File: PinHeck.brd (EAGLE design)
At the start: 359.2 x 152.3 mm, 338 parts, among them IC1 FT232RQ, IC2 PIC32MX7X5FL-PT, IC3 CD74HCT244E, IC4 CD74HCT244E, IC5 ULN2803A, J1 500075-1517, J11 No Load, J2 500075-1517, J6 161-3507-E, P1 TC33X-2-103E, SW1 101-0134-EV, SW2 101-0134-EV, U1 P8X32A-Q44, U10 74HCT2G04GV,125, U11 74HC165D,652, U12 74HC165D,652, U14 MC74HC08ADG, U15 MC74HC08ADG, U16 MC74HC08ADG, U17 MC74HC08ADG, U18 MC74HC08ADG, U19 MC74HC08ADG, U2 FT230X, U20 TIP107, U21 TIP107, U22 TIP107, U23 TIP107, U24 TIP107, U25 TIP107, U26 TIP107, U27 TIP107, U28 TIP102, U29 TIP102, U3 74HC595D-Q100, U30 TIP102, U31 TIP102, U32 TIP102, U33 TIP102, U34 TIP102, U35 TIP102, U36 WS2801, U37 TIP102, U38 WS2801, U4 CAT24M01XI-T2, U40 TIP102, U41 TIP102, U42 TIP102, U43 TIP102, U44 TIP102, U45 TIP102, U46 TIP102, U47 TIP102, U48 TIP102, U49 TIP102, U5 74HC595D-Q100, U50 TIP102, U51 TIP102, U52 CD74HC123M96, U6 TIP102, U7 TIP102, U8 TIP102, U9 TIP102, X1 FQ7050B-8.000, X2 ECS-65-20-4X

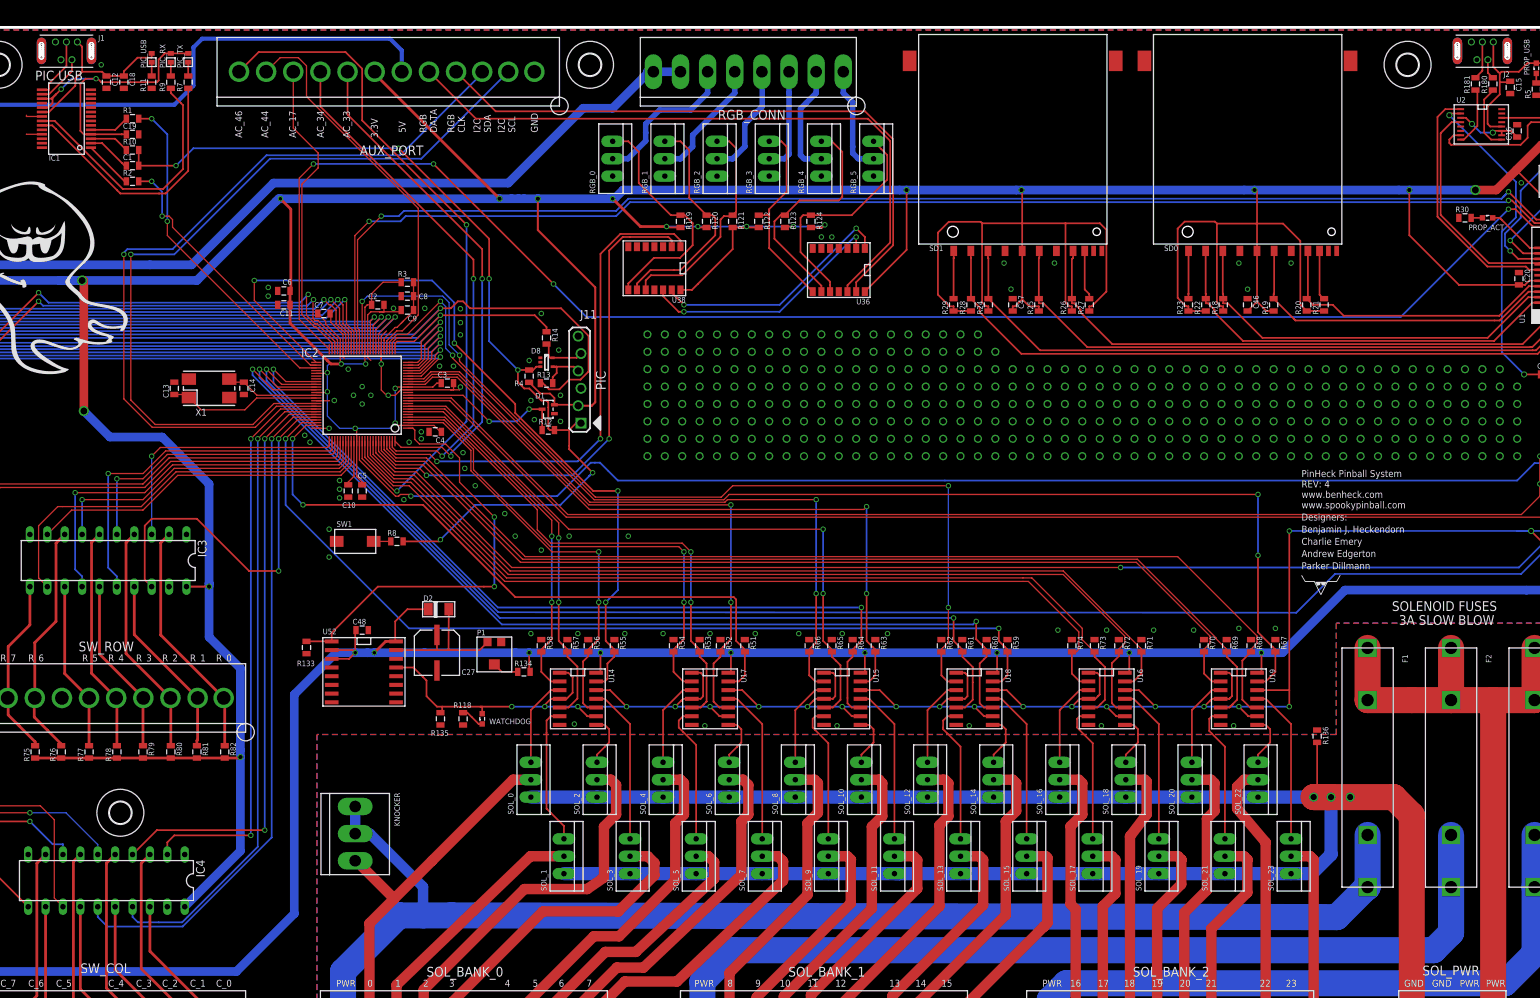
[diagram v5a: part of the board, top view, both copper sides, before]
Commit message: Fixed spacing errors.
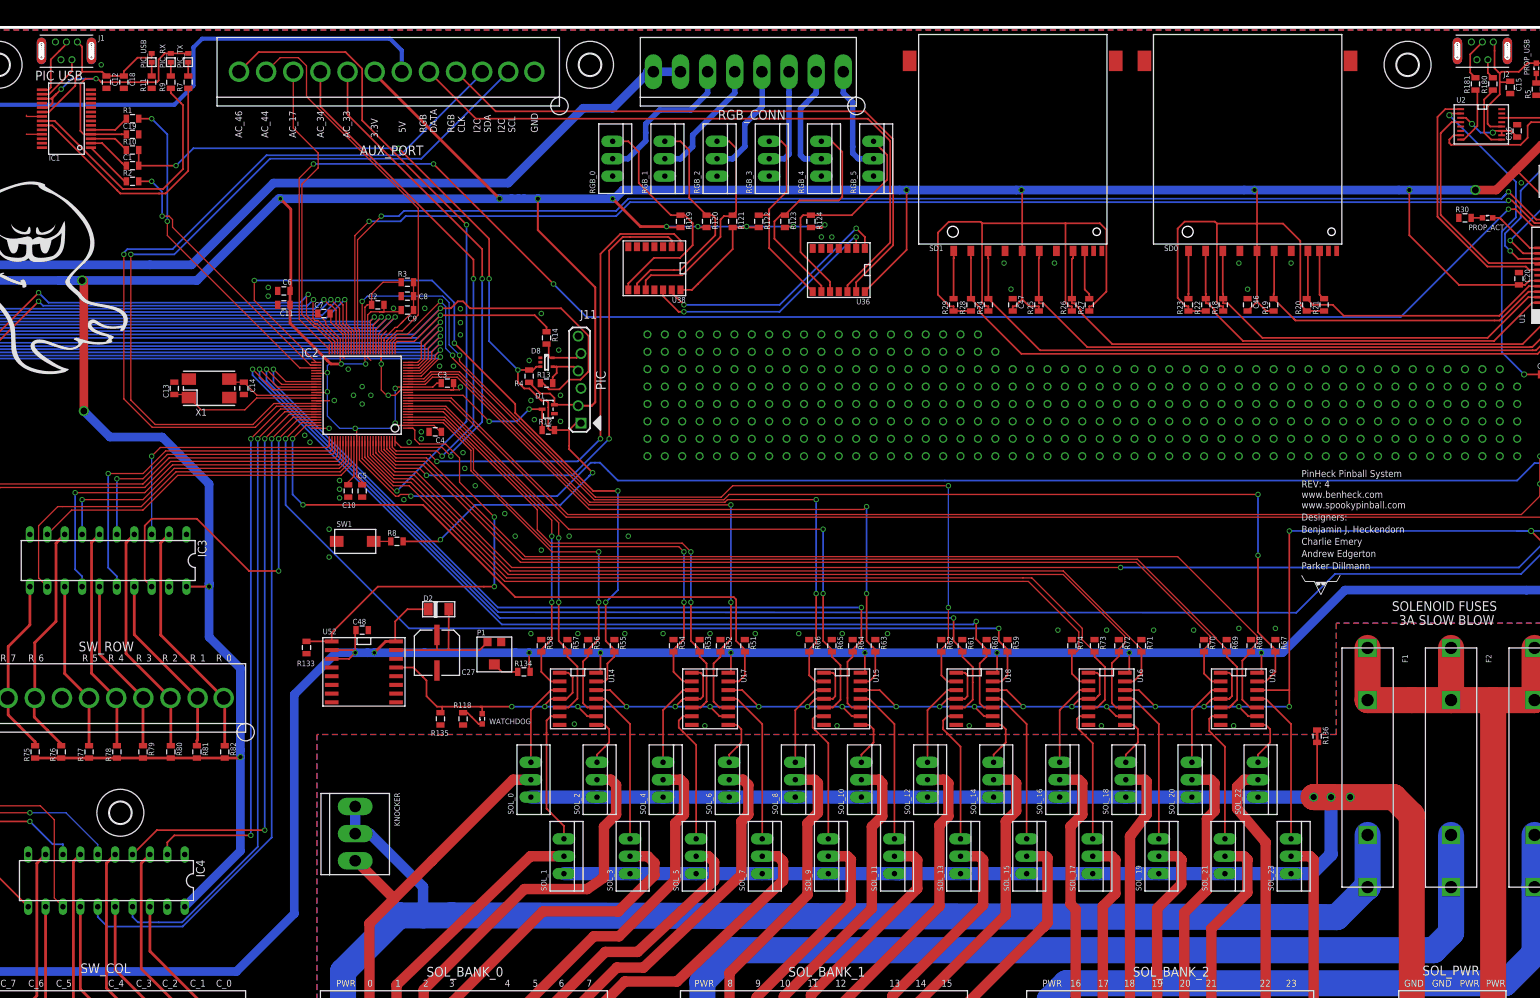
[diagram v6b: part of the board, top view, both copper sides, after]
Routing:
- net N$498: track 0.00 -> 1.78 mm
- net D+: track 5.65 -> 6.28 mm
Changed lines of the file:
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@@
 </class>
 </classes>
-<designrules name="SeeedStudio_2_Layer_DRU">
+<designrules name="Seeed_2_Layer_DRU">
 <description language="de">&lt;b&gt;EAGLE Design Rules&lt;/b&gt;
 &lt;p&gt;
@@
 <contactref element="J1" pad="D+"/>
 <contactref element="IC1" pad="15"/>
-<wire x1="51.289" y1="165.261" x2="52.3185" y2="165.261" width="0.254" layer="1"/>
-<wire x1="54.864" y1="172.242" x2="54.864" y2="168.7175" width="0.254" layer="1"/>
-<wire x1="54.864" y1="168.7175" x2="52.3185" y2="166.172" width="0.254" layer="1"/>
-<wire x1="52.3185" y1="166.172" x2="52.3185" y2="165.261" width="0.254" layer="1"/>
+<wire x1="51.289" y1="165.261" x2="52.231" y2="165.261" width="0.254" layer="1"/>
+<wire x1="52.231" y1="165.261" x2="52.578" y2="165.608" width="0.254" layer="1"/>
+<wire x1="52.578" y1="165.608" x2="52.578" y2="169.672" width="0.254" layer="1"/>
+<wire x1="52.578" y1="169.672" x2="53.848" y2="170.942" width="0.254" layer="1"/>
+<wire x1="53.848" y1="170.942" x2="54.864" y2="171.958" width="0.254" layer="1"/>
+<wire x1="54.864" y1="171.958" x2="54.864" y2="172.242" width="0.254" layer="1"/>
 </signal>
 <signal name="FT_3.3V">
@@
 <contactref element="J2" pad="D+"/>
 <contactref element="R181" pad="2"/>
-<wire x1="261.62" y1="172.242" x2="261.62" y2="168.032" width="0.254" layer="1"/>
-<wire x1="261.62" y1="168.032" x2="260.604" y2="167.016" width="0.254" layer="1"/>
+<wire x1="261.62" y1="172.242" x2="261.62" y2="172.212" width="0.254" layer="1"/>
+<wire x1="261.62" y1="172.212" x2="259.842" y2="170.434" width="0.254" layer="1"/>
+<wire x1="259.842" y1="170.434" x2="259.842" y2="167.778" width="0.254" layer="1"/>
+<wire x1="259.842" y1="167.778" x2="260.604" y2="167.016" width="0.254" layer="1"/>
 </signal>
 <signal name="TXLED">
@@
 <wire x1="262.382" y1="162.814" x2="264.16" y2="164.592" width="0.254" layer="1"/>
 <wire x1="264.16" y1="164.592" x2="264.16" y2="166.37" width="0.254" layer="1"/>
-<wire x1="263.906" y1="167.894" x2="263.22" y2="168.58" width="0.254" layer="1"/>
-<wire x1="263.22" y1="168.58" x2="263.22" y2="172.242" width="0.254" layer="1"/>
+<wire x1="263.906" y1="167.894" x2="263.398" y2="168.402" width="0.254" layer="1"/>
+<wire x1="263.398" y1="168.402" x2="263.398" y2="170.942" width="0.254" layer="1"/>
+<wire x1="263.398" y1="170.942" x2="263.398" y2="172.064" width="0.254" layer="1"/>
+<wire x1="263.398" y1="172.064" x2="263.22" y2="172.242" width="0.254" layer="1"/>
 </signal>
 <signal name="SDA_PROP">
@@
 <contactref element="SOL_BANK_0" pad="P$8"/>
 <wire x1="146.812" y1="53.34" x2="147.6058" y2="53.34" width="1.524" layer="1"/>
-<wire x1="149.4453" y1="50.0457" x2="138.0076" y2="39.37" width="1.524" layer="1"/>
-<wire x1="138.0076" y1="39.37" x2="133.5532" y2="39.37" width="1.524" layer="1"/>
+<wire x1="149.4453" y1="49.7917" x2="138.2616" y2="39.37" width="1.524" layer="1"/>
+<wire x1="138.2616" y1="39.37" x2="133.5532" y2="39.37" width="1.524" layer="1"/>
 <wire x1="133.5532" y1="39.37" x2="122.8852" y2="28.702" width="1.524" layer="1"/>
 <wire x1="147.6058" y1="53.34" x2="148.59" y2="53.34" width="1.524" layer="1"/>
 <wire x1="148.59" y1="53.34" x2="149.4453" y2="52.4847" width="1.524" layer="1"/>
-<wire x1="149.4453" y1="52.4847" x2="149.4453" y2="50.0457" width="1.524" layer="1"/>
+<wire x1="149.4453" y1="52.4847" x2="149.4453" y2="49.7917" width="1.524" layer="1"/>
 </signal>
 <signal name="SOL_PWR_4">
@@
 <wire x1="118.438" y1="80.264" x2="120.766" y2="80.264" width="0.254" layer="1"/>
 </signal>
+<signal name="N$498">
+<wire x1="237.49" y1="70.104" x2="237.49" y2="71.882" width="0.4064" layer="1"/>
+</signal>
 </signals>
+<errors>
+</errors>
 </board>
 </drawing>

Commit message: Fixed Bill of Material Issues
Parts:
- AUX_PORT, CABINET: value (none) -> 26-60-4120
- BOARD_POWER, SOL_PWR: value (none) -> 26-62-4040
- C34, C38, C42, C50: value 100uF -> EEE-1VA101XP
- D1: value BAV99W -> BAV99W,115
- D8: value NSQA6V8 -> NSQA6V8AW5T2G
- DMD_CON: value (none) -> 1-1634688-4
- DMD_PWR: value (none) -> 26-60-4020
- F1, F2, F3: value (none) -> 4245K
- IC1: value FT232RQ -> FT232RQ-REEL
- J3, TCBTWDN_PORT: value (none) -> N/A
- KNOCKER: value (none) -> 26-64-4030
- LIGHT_COL, LIGHT_ROW, SOL_BANK_0, SOL_BANK_1, SOL_BANK_2, SW_COL, SW_ROW: value (none) -> 26-64-4100
- PIC_RX, PIC_TX, PIC_USB, PROP_ACT, PROP_RX, PROP_TX, PROP_USB, PSU_PWR, WATCHDOG: value (none) -> VLMG1500-GS08
- RGB_CONN: value (none) -> 26-60-4080
- SOL_0, SOL_1, SOL_10, SOL_11, SOL_12, SOL_13, SOL_14, SOL_15, SOL_16, SOL_17, SOL_18, SOL_19, SOL_2, SOL_20, SOL_21, SOL_22, SOL_23, SOL_3, SOL_4, SOL_5, SOL_6, SOL_7, SOL_8, SOL_9: value IRL530 -> IRL530PBF
- U2: value FT230X -> FT230XS-R
- U39: value (none) -> LM2937IMP-3.3/NOPB

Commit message: Fixed Part Names
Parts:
- IC2: value PIC32MX7X5FL-PT -> PIC32MX795F512L-80I/PT
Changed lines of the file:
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@@
 <attribute name="NAME" x="52.294" y="154.902" size="0.8128" layer="25" font="vector"/>
 </element>
-<element name="IC2" library="Microchip" package="TQ100-PT" value="PIC32MX7X5FL-PT" x="98.044" y="120.65" rot="R180"/>
+<element name="IC2" library="Microchip" package="TQ100-PT" value="PIC32MX795F512L-80I/PT" x="98.044" y="120.65" rot="R180"/>
 <element name="D1" library="Discrete" package="SOT-323" value="BAV99W,115" x="125.222" y="118.618" smashed="yes" rot="R90">
 <attribute name="NAME" x="123.306" y="120.182" size="0.8128" layer="25"/>
@@
 <element name="PROP_USB" library="led" package="SML0603" value="VLMG1500-GS08" x="269.494" y="168.402" smashed="yes" rot="R90">
 <attribute name="NAME" x="268.494" y="167.402" size="0.8128" layer="25" font="vector" rot="R90"/>
-<attribute name="VALUE" x="271.494" y="167.402" size="1.27" layer="27" rot="R90"/>
 </element>
 <element name="U2" library="PP_DigitalIC" package="SSOP-16" value="FT230XS-R" x="261.62" y="160.528" rot="R270"/>
@@
 <element name="PROP_RX" library="led" package="SML0603" value="VLMG1500-GS08" x="272.288" y="168.402" smashed="yes" rot="R90">
 <attribute name="NAME" x="271.288" y="167.402" size="0.8128" layer="25" font="vector" rot="R90"/>
-<attribute name="VALUE" x="274.288" y="167.402" size="1.27" layer="27" rot="R90"/>
 </element>
 <element name="PROP_TX" library="led" package="SML0603" value="VLMG1500-GS08" x="275.082" y="168.402" smashed="yes" rot="R90">
 <attribute name="NAME" x="274.082" y="167.402" size="0.8128" layer="25" font="vector" rot="R90"/>
-<attribute name="VALUE" x="277.082" y="167.402" size="1.27" layer="27" rot="R90"/>
 </element>
 <element name="R6" library="PP_Passives" package="0805" value="360" x="272.288" y="165.354" rot="R90"/>
@@
 <element name="PSU_PWR" library="led" package="SML0603" value="VLMG1500-GS08" x="37.846" y="163.83" smashed="yes" rot="R270">
 <attribute name="NAME" x="38.624" y="163.306" size="0.8128" layer="25" font="vector"/>
-<attribute name="VALUE" x="35.846" y="164.83" size="1.27" layer="27" rot="R270"/>
 </element>
 <element name="R117" library="PP_Passives" package="0805" value="360" x="37.846" y="167.132" smashed="yes" rot="R270">
@@
 <element name="WATCHDOG" library="led" package="SML0603" value="VLMG1500-GS08" x="115.57" y="73.406" smashed="yes" rot="R90">
 <attribute name="NAME" x="116.602" y="72.628" size="0.8128" layer="25" font="vector"/>
-<attribute name="VALUE" x="117.57" y="72.406" size="1.27" layer="27" rot="R90"/>
 </element>
 <element name="R118" library="PP_Passives" package="0805" value="360" x="112.776" y="73.406" smashed="yes" rot="R270">
